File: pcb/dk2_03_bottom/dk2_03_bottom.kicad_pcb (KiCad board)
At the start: 2 copper layers, 120 x 60 mm, 76 parts, among them J1 Conn_01x20_Pin, J2 Conn_01x16_Pin, J3 Eurorack_Power, J4 Conn_01x20_Pin, J5 Conn_01x20_Pin, J6 Conn_01x03_Pin, Q1 MMBT3904, U1 Pico, U2 AP7333-33SAG, U3 TL072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

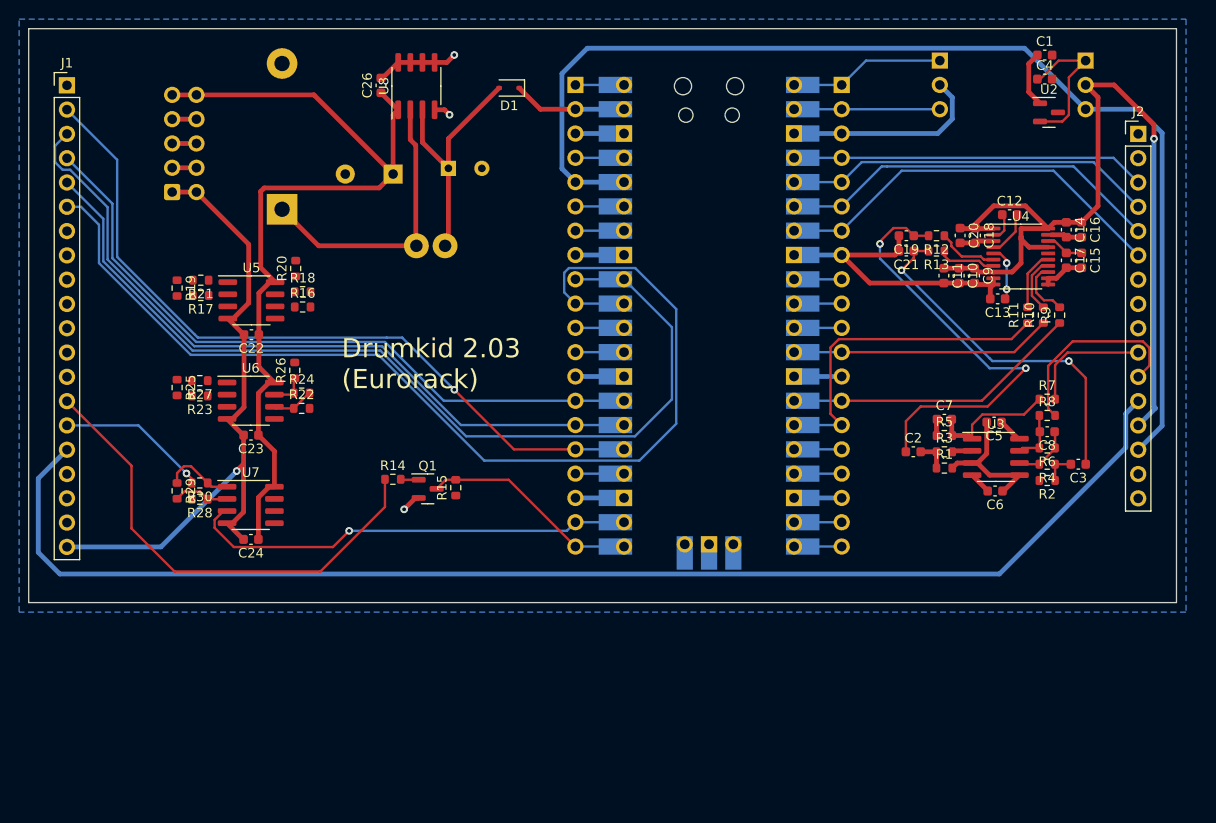
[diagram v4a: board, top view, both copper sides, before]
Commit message: bottom pcb routed
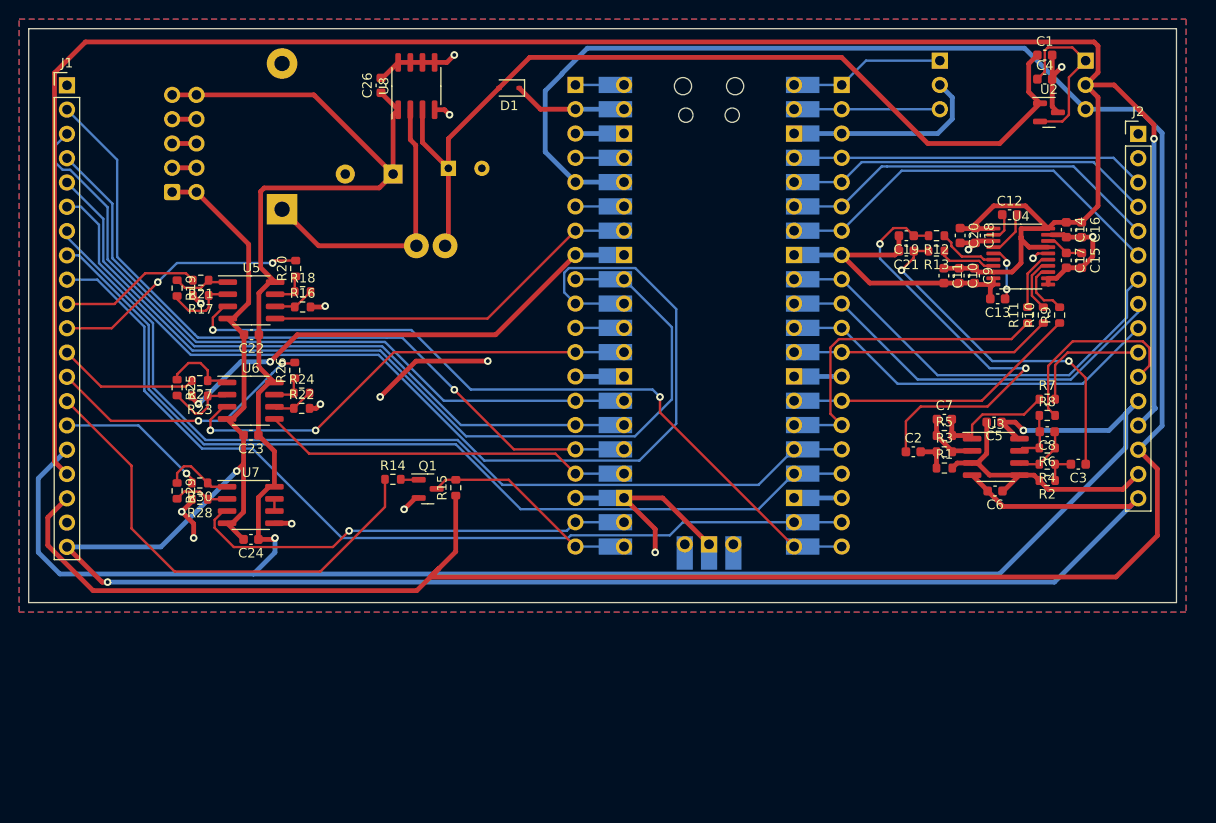
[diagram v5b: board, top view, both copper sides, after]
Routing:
- net +3.3VDAC: track 92.3 -> 250.0 mm
- net +3.3V: track 118.7 -> 266.9 mm
- net -12V: track 71.0 -> 204.9 mm, vias 1 -> 2
- net GND: track 130.1 -> 248.1 mm, vias 3 -> 18
- net 165_LOAD: track 4.98 -> 97.8 mm
- net 165_CLOCK: track 4.98 -> 97.5 mm
- net 165_DATA: track 4.98 -> 96.8 mm
- net TRIGGER_OUT_1: track 4.98 -> 79.4 mm, vias 0 -> 2
- net +5V: track 32.0 -> 95.3 mm
- net TRIGGER_OUT_3: track 5.08 -> 50.0 mm, vias 0 -> 2
- net 595_DATA: track 4.98 -> 45.9 mm
- net 595_CLOCK: track 4.98 -> 43.0 mm
- net 595_LATCH: track 4.98 -> 40.8 mm
- net TRIGGER_OUT_2: track 5.08 -> 40.3 mm
- net TRIGGER_OUT_4: track 5.08 -> 38.9 mm
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- added copper zone on F.Cu, net GND
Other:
- board text added: "Bradshaw Instruments Drumkid 2.03"
- board text removed: "Drumkid 2.03 (Eurorack)"

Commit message: pcbs ordered
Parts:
- moved R1 1.07 mm to (174.8, 96.5)
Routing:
- net GND: track 248.1 -> 233.0 mm, vias 18 -> 17
- net Net-(C2-Pad2): track 3.35 -> 4.22 mm
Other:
- board text added: "TX(Y) GND RX(R)"
- board text removed: "TX GND RX"
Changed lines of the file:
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@@
       (net 72 "+3.3V") (pinfunction "Pin_18") (pintype "passive"))
     (pad "19" thru_hole oval (at 0 45.72) (size 1.7 1.7) (drill 1) (layers "*.Cu" "*.Mask")
-      (net 4 "GND") (pinfunction "Pin_19") (pintype "passive"))
+      (net 4 "GND") (pinfunction "Pin_19") (pintype "passive") (thermal_bridge_angle 45))
     (pad "20" thru_hole oval (at 0 48.26) (size 1.7 1.7) (drill 1) (layers "*.Cu" "*.Mask")
       (net 60 "-12V") (pinfunction "Pin_20") (pintype "passive"))
@@
   )
   (footprint "Resistor_SMD:R_0603_1608Metric" (layer "F.Cu")
-    (at 175.735 95.935)
+    (at 174.825 96.5)
     (descr "Resistor SMD 0603 (1608 Metric), square (rectangular) end terminal, IPC_7351 nominal, (Body size source: IPC-SM-782 page 72, https://www.pcb-3d.com/wordpress/wp-content/uploads/ipc-sm-782a_amendment_1_and_2.pdf), generated with kicad-footprint-generator")
     (tags "resistor")
@@
       (net 1 "Net-(C2-Pad2)") (pintype "passive"))
     (pad "2" smd roundrect (at 0.825 0) (size 0.8 0.95) (layers "F.Cu" "F.Paste" "F.Mask") (roundrect_rratio 0.25)
-      (net 4 "GND") (pintype "passive"))
+      (net 4 "GND") (pintype "passive") (thermal_bridge_angle 45))
     (model "${KICAD6_3DMODEL_DIR}/Resistor_SMD.3dshapes/R_0603_1608Metric.wrl"
       (offset (xyz 0 0 0))
@@
       (net 39 "SERIAL_TX") (pinfunction "Pin_1") (pintype "passive"))
     (pad "2" thru_hole oval (at 0 -2.54 180) (size 1.7 1.7) (drill 1) (layers "*.Cu" "*.Mask")
-      (net 4 "GND") (pinfunction "Pin_2") (pintype "passive"))
+      (net 4 "GND") (pinfunction "Pin_2") (pintype "passive") (thermal_bridge_angle 45))
     (pad "3" thru_hole oval (at 0 -5.08 180) (size 1.7 1.7) (drill 1) (layers "*.Cu" "*.Mask")
       (net 73 "SERIAL_RX") (pinfunction "Pin_3") (pintype "passive"))
@@
       (net 16 "Net-(#FLG02-pwr)") (pinfunction "Pin_2") (pintype "passive"))
     (pad "3" thru_hole oval (at 0 -5.08 180) (size 1.7 1.7) (drill 1) (layers "*.Cu" "*.Mask")
-      (net 4 "GND") (pinfunction "Pin_3") (pintype "passive"))
+      (net 4 "GND") (pinfunction "Pin_3") (pintype "passive") (thermal_bridge_angle 45))
     (pad "4" thru_hole oval (at 0 -7.62 180) (size 1.7 1.7) (drill 1) (layers "*.Cu" "*.Mask")
       (net 75 "unconnected-(J5-Pin_4-Pad4)") (pinfunction "Pin_4") (pintype "passive"))
@@
       (net 77 "TRIGGER_OUT_4") (pinfunction "Pin_17") (pintype "passive"))
     (pad "18" thru_hole oval (at 0 -43.18 180) (size 1.7 1.7) (drill 1) (layers "*.Cu" "*.Mask")
-      (net 4 "GND") (pinfunction "Pin_18") (pintype "passive"))
+      (net 4 "GND") (pinfunction "Pin_18") (pintype "passive") (thermal_bridge_angle 45))
     (pad "19" thru_hole oval (at 0 -45.72 180) (size 1.7 1.7) (drill 1) (layers "*.Cu" "*.Mask")
       (net 30 "SYNC_OUT") (pinfunction "Pin_19") (pintype "passive"))
@@
       (net 42 "unconnected-(U1-SWCLK-Pad41)") (pinfunction "SWCLK") (pintype "input+no_connect"))
     (pad "42" thru_hole rect (at 0 -23.9 180) (size 1.7 1.7) (drill 1.02) (layers "*.Cu" "*.Mask")
-      (net 4 "GND") (pinfunction "GND") (pintype "power_in"))
+      (net 4 "GND") (pinfunction "GND") (pintype "power_in") (thermal_bridge_angle 45))
     (pad "42" smd rect (at 0 -23.9 90) (size 3.5 1.7) (drill (offset -0.9 0)) (layers "B.Cu" "B.Mask")
       (net 4 "GND") (pinfunction "GND") (pintype "power_in"))
@@
     (effects (font (size 2.5 2.5) (thickness 0.2)) (justify left bottom mirror))
   )
-  (gr_text "TX\nGND\nRX" (at 173 59) (layer "B.SilkS")
+  (gr_text "TX(Y)\nGND\nRX(R)" (at 173 59) (layer "B.SilkS")
     (effects (font (size 1.5 1.5) (thickness 0.3) bold) (justify left bottom mirror))
   )
@@
   )
   (segment (start 174.91 94.235) (end 173.26 94.235) (width 0.5) (layer "F.Cu") (net 1))
-  (segment (start 174.91 95.935) (end 174.91 94.235) (width 0.5) (layer "F.Cu") (net 1))
+  (segment (start 173.26 95.76) (end 173.26 94.235) (width 0.25) (layer "F.Cu") (net 1))
+  (segment (start 174 96.5) (end 173.26 95.76) (width 0.25) (layer "F.Cu") (net 1))
   (segment (start 187.31 95.535) (end 187.31 97.235) (width 0.25) (layer "F.Cu") (net 2))
   (segment (start 188.96 95.535) (end 187.31 95.535) (width 0.25) (layer "F.Cu") (net 2))
@@
   (segment (start 123.725 53.525) (end 124.5 52.75) (width 0.5) (layer "F.Cu") (net 4))
   (segment (start 105.69 101.7) (end 107.45 101.7) (width 0.5) (layer "F.Cu") (net 4))
-  (segment (start 178.635 95.405) (end 177.09 95.405) (width 0.5) (layer "F.Cu") (net 4))
   (segment (start 187.005 55.27) (end 187.005 58.1475) (width 0.5) (layer "F.Cu") (net 4))
   (segment (start 165 73.66) (end 170.5675 73.66) (width 0.5) (layer "F.Cu") (net 4))
@@
   (segment (start 167.935 76.595) (end 165 73.66) (width 0.5) (layer "F.Cu") (net 4))
   (segment (start 170.9825 73.245) (end 170.9825 71.645) (width 0.5) (layer "F.Cu") (net 4))
+  (segment (start 175.65 96.5) (end 176.745 95.405) (width 0.5) (layer "F.Cu") (net 4))
   (segment (start 188.4825 71.795) (end 188.2325 71.545) (width 0.5) (layer "F.Cu") (net 4))
   (segment (start 181.925 98.335) (end 183.585 96.675) (width 0.5) (layer "F.Cu") (net 4))
@@
   (segment (start 187.005 52.76) (end 187.005 55.27) (width 0.5) (layer "F.Cu") (net 4))
   (segment (start 175.6825 76.595) (end 167.935 76.595) (width 0.5) (layer "F.Cu") (net 4))
-  (segment (start 177.09 95.405) (end 176.56 95.935) (width 0.5) (layer "F.Cu") (net 4))
   (segment (start 180.5325 77.07) (end 180.8575 76.745) (width 0.5) (layer "F.Cu") (net 4))
+  (segment (start 176.745 95.405) (end 178.635 95.405) (width 0.5) (layer "F.Cu") (net 4))
   (via (at 97.75 89.25) (size 0.8) (drill 0.4) (layers "F.Cu" "B.Cu") (net 4))
   (via (at 119.25 100.25) (size 0.8) (drill 0.4) (layers "F.Cu" "B.Cu") (net 4))
   (via (at 97.25 103.25) (size 0.8) (drill 0.4) (layers "F.Cu" "B.Cu") (free) (net 4))
-  (via (at 96 100.5) (size 0.8) (drill 0.4) (layers "F.Cu" "B.Cu") (net 4))
   (via (at 188 54) (size 0.8) (drill 0.4) (layers "F.Cu" "B.Cu") (net 4))
   (via (at 185 74) (size 0.8) (drill 0.4) (layers "F.Cu" "B.Cu") (net 4))
@@
   (segment (start 160.02 73.66) (end 165 73.66) (width 0.5) (layer "B.Cu") (net 4))
   (segment (start 160.02 60.96) (end 165 60.96) (width 0.5) (layer "B.Cu") (net 4))
-  (segment (start 176.56 59.44) (end 175.04 60.96) (width 0.5) (layer "B.Cu") (net 4))
   (segment (start 137.16 60.96) (end 142.24 60.96) (width 0.5) (layer "B.Cu") (net 4))
   (segment (start 165 99.06) (end 160.02 99.06) (width 0.5) (layer "B.Cu") (net 4))
@@
   (segment (start 102.1755 84.8245) (end 105.25 84.8245) (width 0.5) (layer "B.Cu") (net 4))
   (segment (start 160.02 86.36) (end 165 86.36) (width 0.5) (layer "B.Cu") (net 4))
-  (segment (start 175.26 55.88) (end 176.56 57.18) (width 0.5) (layer "B.Cu") (net 4))
-  (segment (start 176.56 57.18) (end 176.56 59.44) (width 0.5) (layer "B.Cu") (net 4))
   (segment (start 137.16 86.36) (end 142.24 86.36) (width 0.5) (layer "B.Cu") (net 4))
-  (segment (start 175.04 60.96) (end 165 60.96) (width 0.5) (layer "B.Cu") (net 4))
   (segment (start 130.18 97.16) (end 137.16 104.14) (width 0.25) (layer "F.Cu") (net 5))
   (segment (start 123.6 97.16) (end 122.65 98.11) (width 0.25) (layer "F.Cu") (net 5))
